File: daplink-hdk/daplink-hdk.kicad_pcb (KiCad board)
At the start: 2 copper layers, 90 x 65 mm, 68 parts, among them J1 USB_C_Receptacle_USB2.0, J2 Conn_02x05_Odd_Even, J3 Conn_01x12_Socket, J4 Conn_02x05_Odd_Even, J5 Conn_01x12_Socket, J6 Conn_01x03, Q1 DMP3099L, Q3 DMN3023L-7, SW1 SW_Push, SW2 SW_Push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

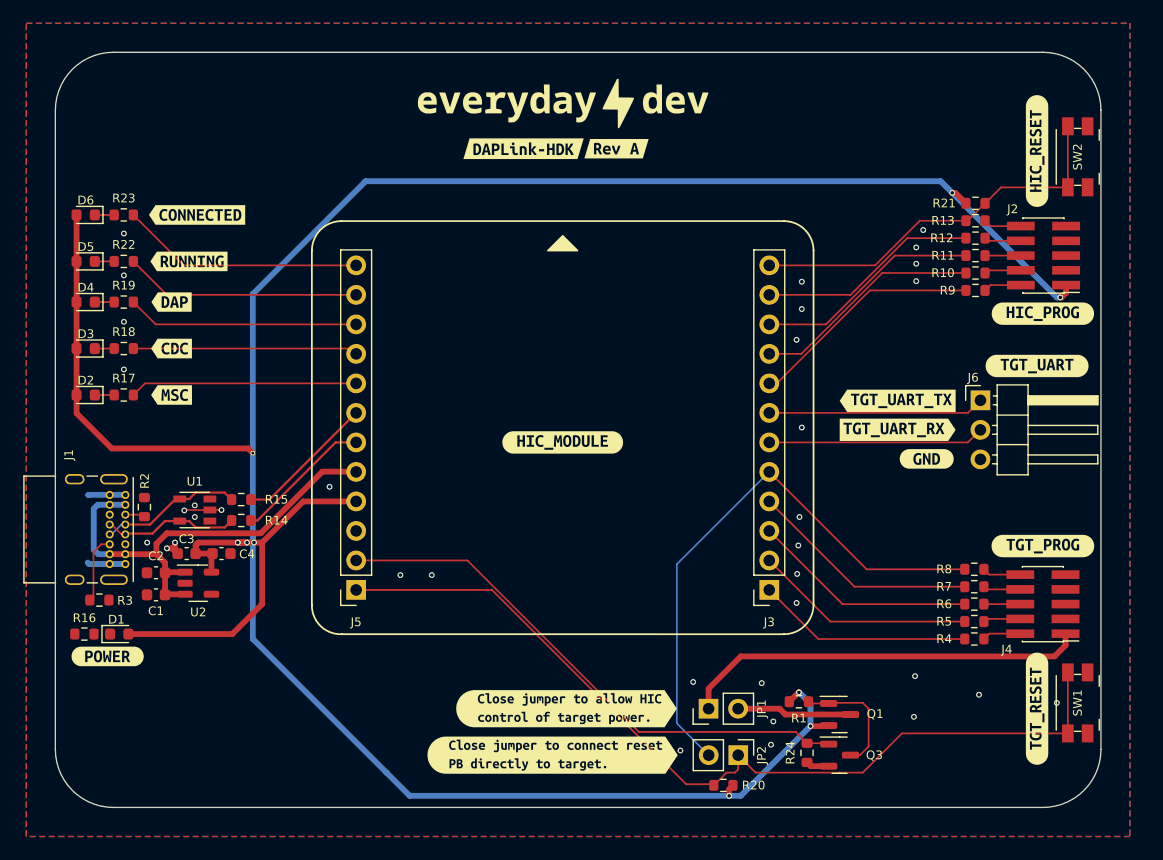
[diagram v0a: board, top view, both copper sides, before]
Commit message: Fix missing power LED trace, increment rev, and add Gitlab CI
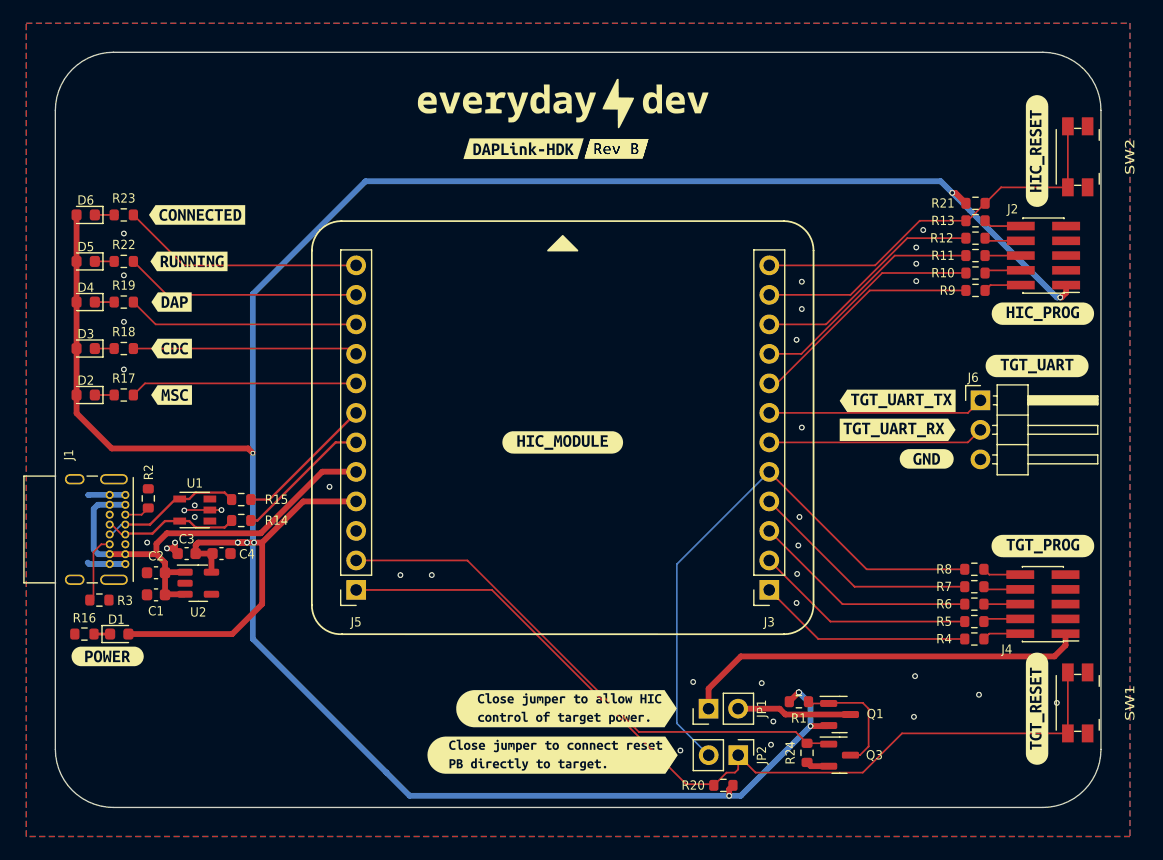
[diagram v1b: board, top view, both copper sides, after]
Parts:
- removed kibuzzard-6548E80B: G***, kibuzzard-6548E80B
- added kibuzzard-65CA74FC: G***, kibuzzard-65CA74FC, F.Cu at (158.3, 43.3)
- added kibuzzard-65CA7DAF: G***, kibuzzard-65CA7DAF, F.Cu at (158.3, 43.3)
- moved R2 0.82 mm to (118.0, 73.4)
- turned R20 to 0 degrees
- turned R21 to 180 degrees
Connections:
- R20 pad 1: +3V3 -> /TGT_nRESET_FWRD
- R20 pad 2: /TGT_nRESET_FWRD -> +3V3
- R21 pad 1: +3V3 -> /HIC_nRESET
- R21 pad 2: /HIC_nRESET -> +3V3
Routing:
- net Net-(D1-K): track 0.00 -> 1.39 mm
- net Net-(J1-CC1): track 1.70 -> 2.21 mm
- net +3V3: vias 9 -> 10
